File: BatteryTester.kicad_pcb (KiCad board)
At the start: 2 copper layers, 68.6 x 53.3 mm, 24 parts, among them P1 CONN_01X02, P2 CONN_01X04, Q1 MOSFET_N, Q2 MOSFET_N, Q3 MOSFET_N, Q4 MOSFET_N

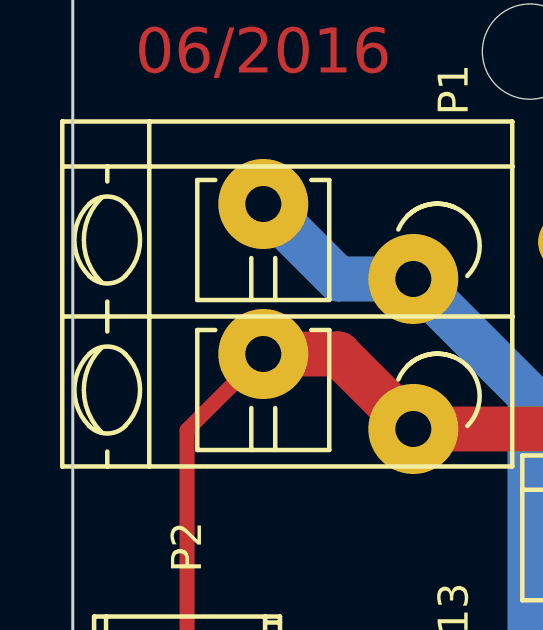
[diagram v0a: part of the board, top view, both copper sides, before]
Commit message: Update to KiCad 6
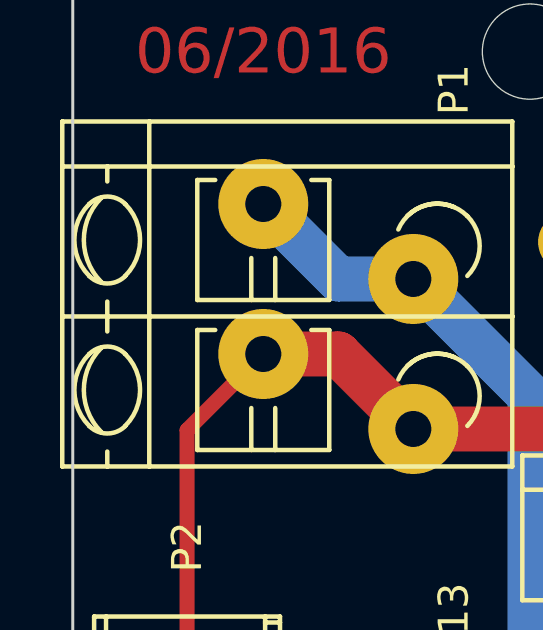
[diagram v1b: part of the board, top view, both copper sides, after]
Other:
- net class Default removed
- net class Power removed
